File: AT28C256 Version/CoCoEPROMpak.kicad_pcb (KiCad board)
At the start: 2 copper layers, 53.3 x 44.5 mm, 8 parts, among them P1 COCO-CART, U1 2732, U2 28C256

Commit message: Added gerber files
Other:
- board text added: "AT28C256 Version by RCC @ 2023 https://github.com/costarc/CoCoEPROMpak"
- board text added: "RCC@2023"
- board text added: "Rev 0"
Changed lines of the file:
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@@
       (outputformat 1)
       (mirror false)
-      (drillshape 1)
+      (drillshape 0)
       (scaleselection 1)
-      (outputdirectory "")
+      (outputdirectory "Fabrication/")
     )
   )
@@
       (effects (font (size 1.63576 1.63576) (thickness 0.14224)) (justify left bottom))
     )
-    (fp_text value "COCO-CART" (at 0 0) (layer "F.Fab")
+    (fp_text value "COCO-CART" (at -7.509874 -12.893544) (layer "F.Fab") hide
       (effects (font (size 1.27 1.27) (thickness 0.15)))
     )
@@
       (net 4 "Net-(JP1-Pad2)") (pinfunction "2") (pintype "passive") (solder_mask_margin 0.0762))
   )
+  (gr_text "AT28C256 Version by RCC @ 2023\nhttps://github.com/costarc/CoCoEPROMpak" (at 166.400839 90.472996) (layer "B.SilkS")
+    (effects (font (size 0.7 0.7) (thickness 0.15)) (justify left mirror))
+  )
   (gr_text "CoCoEPROMpak v1\nCopyright 2013 by Mark J. Blair\nDistributed under GPLv3\nhttps://github.com/NF6X/CoCoEPROMpak" (at 166.841816 105.693718) (layer "B.SilkS")
     (effects (font (size 1.2 1.2) (thickness 0.113792)) (justify left bottom mirror))
@@
     (effects (font (size 0.6 0.6) (thickness 0.1016)) (justify left bottom))
   )
+  (gr_text "RCC@2023" (at 125.449759 113.223596) (layer "F.SilkS")
+    (effects (font (size 0.7 0.7) (thickness 0.15)))
+  )
   (gr_text "A15" (at 170.434216 89.907074) (layer "F.SilkS")
     (effects (font (size 0.6 0.6) (thickness 0.15)))
@@
     (effects (font (size 0.6 0.6) (thickness 0.15)) (justify left))
   )
+  (gr_text "Rev 0" (at 165.887115 86.069654) (layer "F.SilkS")
+    (effects (font (size 1 1) (thickness 0.15)))
+  )
   (gr_text "CoCoEPROMpak\nby NF6X" (at 154.426672 86.639262) (layer "F.Mask")

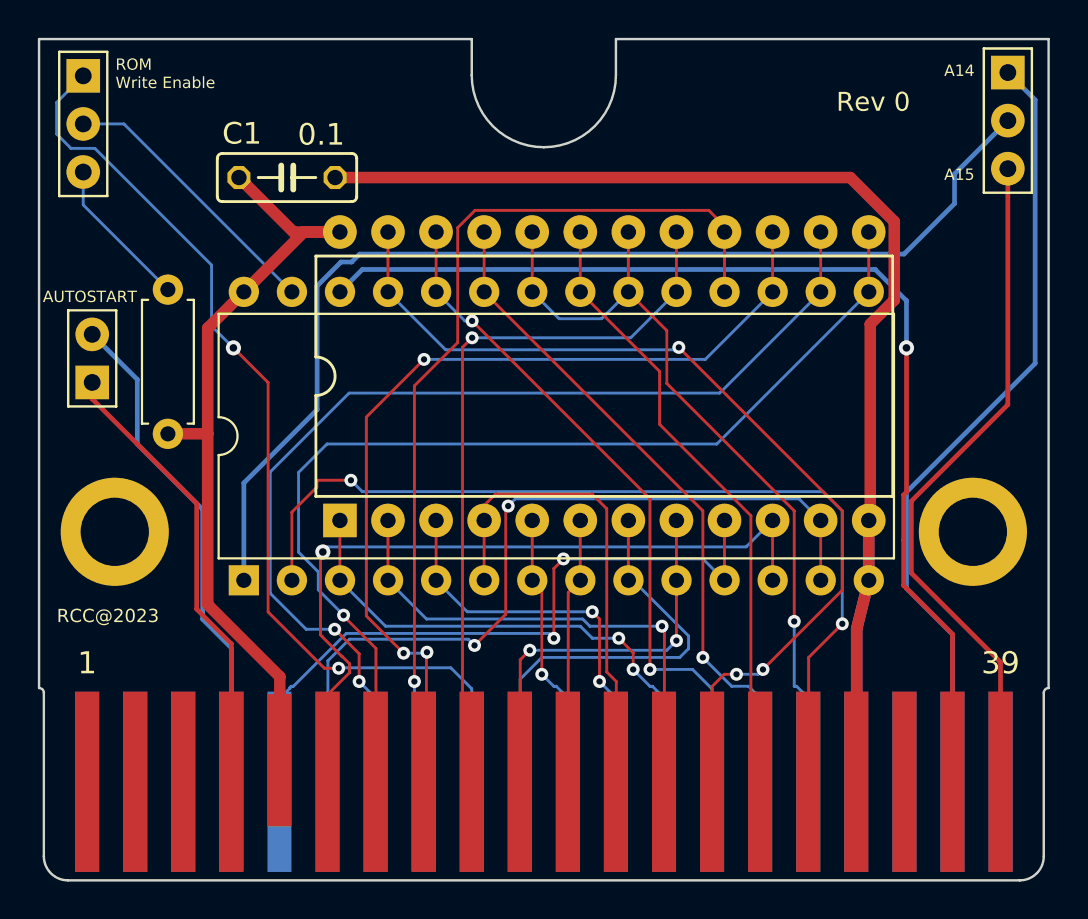
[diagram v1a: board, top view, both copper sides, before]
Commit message: Added gerbers with gnd plane added
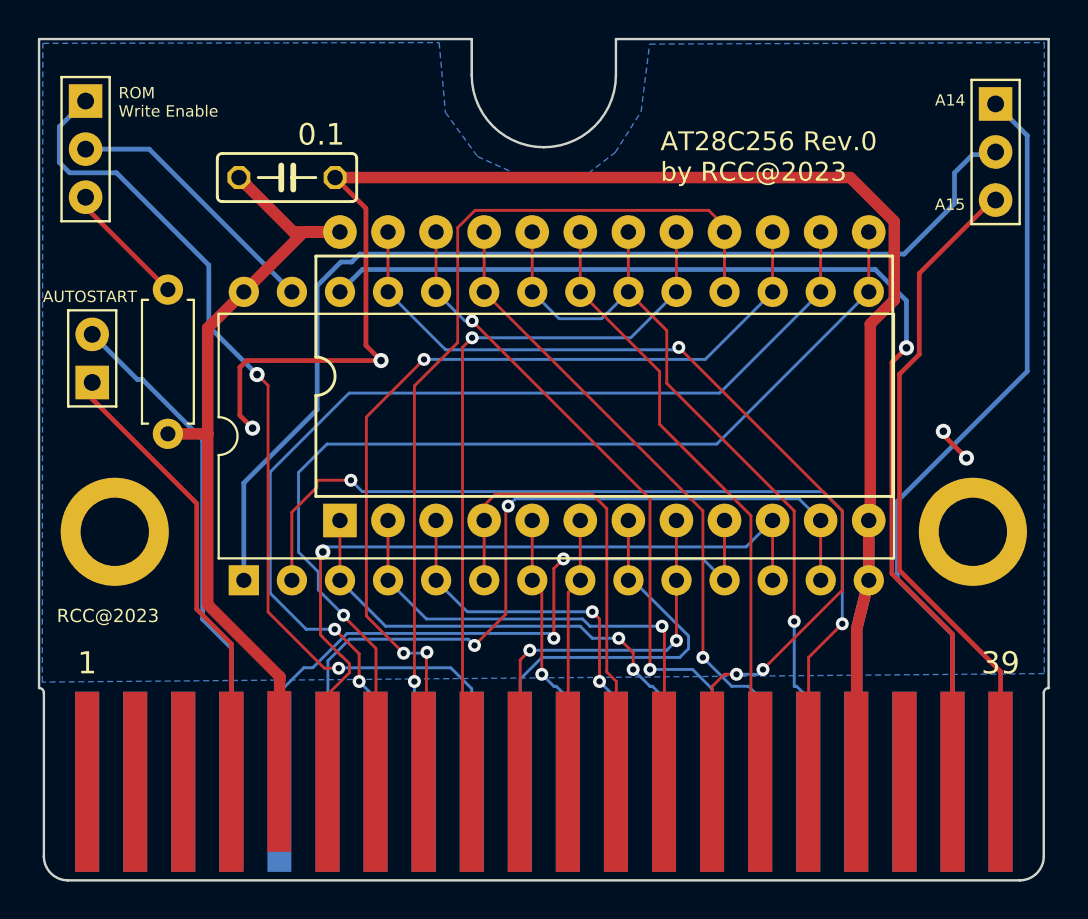
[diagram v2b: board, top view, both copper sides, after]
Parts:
- JP1: value JP1 -> JP2
- P1: footprint CoCoEPROMpak:COCO-CART-2.1X1.75 -> Roni Footprints:COCO-CART-2.1X1.75
- moved JP2 1.78 mm to (172.3, 86.2)
- moved JP3 1.34 mm to (124.3, 86.0)
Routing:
- net GND: track 74.7 -> 98.4 mm, vias 0 -> 4
- net Net-(JP3-Pad3): track 8.07 -> 6.68 mm
- net A14: track 41.9 -> 40.6 mm
- net A15: track 36.5 -> 35.1 mm
- net ROM_A14: track 58.2 -> 56.9 mm
- net *WE: track 14.7 -> 14.0 mm
- net *RW: track 51.6 -> 51.0 mm
- net +5V: track 42.2 -> 42.7 mm
- net /A13: track 57.6 -> 58.2 mm
- added copper zone on B.Cu, net GND
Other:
- board text added: "AT28C256 Rev.0 by RCC@2023"
- board text removed: "Rev 0"

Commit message: Rev.1
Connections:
- JP2 pad 1: A14 -> GND
- JP2 pad 3: A15 -> +5V
- P1 pad 38: A14 -> unconnected-(P1-Pad38)
- P1 pad 39: A15 -> unconnected-(P1-Pad39)
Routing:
- net +5V: track 42.7 -> 84.1 mm
- net A14: track 40.6 -> 0.00 mm
- net A15: track 35.1 -> 0.00 mm
- net GND: track 98.4 -> 123.1 mm, vias 4 -> 2
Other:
- board text added: "AT28C256 Rev.1 by RCC@2023"
- board text removed: "AT28C256 Rev.0 by RCC@2023"
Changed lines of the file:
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@@
   )
   (paper "A4")
+  (title_block
+    (date "2023-02-12")
+  )
   (layers
     (0 "F.Cu" signal)
@@
   (net 3 "Net-(JP1-Pad1)")
   (net 4 "Net-(JP1-Pad2)")
-  (net 5 "A14")
+  (net 5 "unconnected-(P1-Pad38)")
   (net 6 "ROM_A14")
-  (net 7 "A15")
+  (net 7 "unconnected-(P1-Pad39)")
   (net 8 "*RW")
   (net 9 "*WE")
@@
     (fp_line (start -1.27 6.35) (end -1.27 -1.27) (layer "F.SilkS") (width 0.127))
     (pad "1" thru_hole rect (at 0 0) (size 1.778 1.778) (drill 0.889) (layers *.Cu *.Mask)
-      (net 5 "A14") (pinfunction "1") (pintype "passive") (solder_mask_margin 0.0762))
+      (net 1 "GND") (pinfunction "1") (pintype "passive") (solder_mask_margin 0.0762))
     (pad "2" thru_hole circle (at 0 2.54) (size 1.778 1.778) (drill 0.889) (layers *.Cu *.Mask)
       (net 6 "ROM_A14") (pinfunction "2") (pintype "passive") (solder_mask_margin 0.0762))
     (pad "3" thru_hole circle (at 0 5.08) (size 1.778 1.778) (drill 0.889) (layers *.Cu *.Mask)
-      (net 7 "A15") (pinfunction "3") (pintype "passive") (solder_mask_margin 0.0762))
+      (net 2 "+5V") (pinfunction "3") (pintype "passive") (solder_mask_margin 0.0762))
   )
   (footprint "CoCoEPROMpak:C050-025X075" (layer "F.Cu")
@@
       (net 40 "/A13") (pinfunction "A13") (pintype "output") (solder_mask_margin 0.0762))
     (pad "38" smd rect (at 48.26 -5.207) (size 1.27 9.525) (layers "B.Cu" "B.Mask")
-      (net 5 "A14") (pinfunction "A14") (pintype "output") (solder_mask_margin 0.0762))
+      (net 5 "unconnected-(P1-Pad38)") (pinfunction "A14") (pintype "output+no_connect") (solder_mask_margin 0.0762))
     (pad "39" smd rect (at 50.8 -5.207) (size 1.27 9.525) (layers "F.Cu" "F.Mask")
-      (net 7 "A15") (pinfunction "A15") (pintype "output") (solder_mask_margin 0.0762))
+      (net 7 "unconnected-(P1-Pad39)") (pinfunction "A15") (pintype "output+no_connect") (solder_mask_margin 0.0762))
     (pad "40" smd rect (at 50.8 -5.207) (size 1.27 9.525) (layers "B.Cu" "B.Mask")
       (net 41 "unconnected-(P1-Pad40)") (pinfunction "~{SLENB}") (pintype "input") (solder_mask_margin 0.0762))
@@
     (effects (font (size 0.6 0.6) (thickness 0.15)) (justify left))
   )
-  (gr_text "AT28C256 Rev.0 \nby RCC@2023" (at 154.64 88.96) (layer "F.SilkS")
+  (gr_text "AT28C256 Rev.1\nby RCC@2023" (at 154.64 88.96) (layer "F.SilkS")
     (effects (font (size 1 1) (thickness 0.15)) (justify left))
   )
@@
   (segment (start 139.88 99.73) (end 132.78 99.73) (width 0.25) (layer "F.Cu") (net 1))
   (segment (start 164.671336 90.060021) (end 137.451251 90.060021) (width 0.6096) (layer "F.Cu") (net 1))
-  (segment (start 169.59 103.66) (end 170.81 104.88) (width 0.25) (layer "F.Cu") (net 1))
   (segment (start 139.0797 98.9297) (end 139.0797 91.68847) (width 0.25) (layer "F.Cu") (net 1))
-  (segment (start 169.59 103.47) (end 169.59 103.66) (width 0.25) (layer "F.Cu") (net 1))
   (segment (start 139.88 99.73) (end 139.0797 98.9297) (width 0.25) (layer "F.Cu") (net 1))
   (segment (start 165.6461 108.1786) (end 165.726883 108.097817) (width 0.6096) (layer "F.Cu") (net 1))
@@
   (via (at 139.88 99.73) (size 0.8) (drill 0.4) (layers "F.Cu" "B.Cu") (free) (net 1))
   (via (at 133.09 103.3) (size 0.8) (drill 0.4) (layers "F.Cu" "B.Cu") (free) (net 1))
-  (via (at 170.81 104.88) (size 0.8) (drill 0.4) (layers "F.Cu" "B.Cu") (free) (net 1))
-  (via (at 169.59 103.47) (size 0.8) (drill 0.4) (layers "F.Cu" "B.Cu") (free) (net 1))
+  (segment (start 173.736 94.234) (end 173.736 86.36) (width 0.6096) (layer "B.Cu") (net 1))
+  (segment (start 173.736 86.36) (end 173.546 86.17) (width 0.6096) (layer "B.Cu") (net 1))
+  (segment (start 173.546 86.17) (end 172.35 86.17) (width 0.6096) (layer "B.Cu") (net 1))
   (segment (start 165.0111 113.8936) (end 165.6461 111.3536) (width 0.6096) (layer "B.Cu") (net 1))
   (segment (start 165.6461 108.1786) (end 165.6461 111.3536) (width 0.6096) (layer "B.Cu") (net 1))
   (segment (start 165.0111 122.0216) (end 165.0111 113.8936) (width 0.6096) (layer "B.Cu") (net 1))
+  (segment (start 165.6461 102.3239) (end 173.736 94.234) (width 0.6096) (layer "B.Cu") (net 1))
+  (segment (start 165.6461 108.1786) (end 165.6461 102.3239) (width 0.6096) (layer "B.Cu") (net 1))
   (segment (start 130.7211 103.590222) (end 130.7211 98.0186) (width 0.6096) (layer "F.Cu") (net 2))
   (segment (start 135.8011 92.9386) (end 132.6261 96.1136) (width 0.6096) (layer "F.Cu") (net 2))
   (segment (start 130.7211 103.590222) (end 130.709898 103.601424) (width 0.6096) (layer "F.Cu") (net 2))
   (segment (start 130.7211 98.0186) (end 132.6261 96.1136) (width 0.6096) (layer "F.Cu") (net 2))
+  (segment (start 172.35 91.25) (end 166.684671 91.25) (width 0.25) (layer "F.Cu") (net 2))
+  (segment (start 133.531272 88.9) (end 132.371251 90.060021) (width 0.25) (layer "F.Cu") (net 2))
   (segment (start 135.24983 92.9386) (end 132.371251 90.060021) (width 0.6096) (layer "F.Cu") (net 2))
   (segment (start 134.5311 116.4336) (end 134.521844 116.442856) (width 0.6096) (layer "F.Cu") (net 2))
+  (segment (start 166.684671 91.25) (end 164.334671 88.9) (width 0.25) (layer "F.Cu") (net 2))
+  (segment (start 164.334671 88.9) (end 133.531272 88.9) (width 0.25) (layer "F.Cu") (net 2))
   (segment (start 130.7211 112.6236) (end 130.7211 103.590222) (width 0.6096) (layer "F.Cu") (net 2))
   (segment (start 130.709898 103.601424) (end 128.617205 103.601424) (width 0.6096) (layer "F.Cu") (net 2))
@@
   (segment (start 127 100.727658) (end 127.267113 100.727658) (width 0.25) (layer "B.Cu") (net 4))
   (segment (start 130.455428 113.400012) (end 131.969874 114.914458) (width 0.25) (layer "B.Cu") (net 4))
-  (segment (start 174.02 87.84) (end 172.35 86.17) (width 0.25) (layer "B.Cu") (net 5))
-  (segment (start 167.16 111.28) (end 167.16 107.16) (width 0.25) (layer "B.Cu") (net 5))
-  (segment (start 170.069874 114.189874) (end 167.16 111.28) (width 0.25) (layer "B.Cu") (net 5))
-  (segment (start 170.069874 121.986544) (end 170.069874 114.189874) (width 0.25) (layer "B.Cu") (net 5))
-  (segment (start 167.16 107.16) (end 174.02 100.3) (width 0.25) (layer "B.Cu") (net 5))
-  (segment (start 174.02 100.3) (end 174.02 87.84) (width 0.25) (layer "B.Cu") (net 5))
   (segment (start 170.18 91.44) (end 170.18 89.81) (width 0.25) (layer "B.Cu") (net 6))
   (segment (start 172.21 88.85) (end 172.35 88.71) (width 0.25) (layer "B.Cu") (net 6))
@@
   (segment (start 136.503658 102.322253) (end 136.503658 95.781311) (width 0.25) (layer "B.Cu") (net 6))
   (segment (start 132.629265 111.341512) (end 132.629265 106.196646) (width 0.25) (layer "B.Cu") (net 6))
-  (segment (start 172.609874 116.160794) (end 172.609874 121.986544) (width 0.25) (layer "F.Cu") (net 7))
-  (segment (start 172.35 91.25) (end 172.19 91.25) (width 0.25) (layer "F.Cu") (net 7))
-  (segment (start 168.3174 95.1226) (end 168.3174 99.4026) (width 0.25) (layer "F.Cu") (net 7))
-  (segment (start 167.2724 100.4476) (end 167.2724 110.82332) (width 0.25) (layer "F.Cu") (net 7))
-  (segment (start 172.19 91.25) (end 168.3174 95.1226) (width 0.25) (layer "F.Cu") (net 7))
-  (segment (start 167.2724 110.82332) (end 172.609874 116.160794) (width 0.25) (layer "F.Cu") (net 7))
-  (segment (start 168.3174 99.4026) (end 167.2724 100.4476) (width 0.25) (layer "F.Cu") (net 7))
   (segment (start 136.883757 115.986173) (end 137.6421 115.986173) (width 0.1524) (layer "F.Cu") (net 8))
   (segment (start 133.909408 101.049408) (end 133.909408 113.011824) (width 0.1524) (layer "F.Cu") (net 8))
